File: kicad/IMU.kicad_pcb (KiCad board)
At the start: 4 copper layers, 37.6 x 37.6 mm, 89 parts, among them IC1 FT232RQ, P1 M1P, P10 CONN_01X02, P11 CONN_02X05, P12 CONN_02X06, P2 M1N, P3 M3P, P4 M3N, P5 JTAG_DB, P6 M2P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

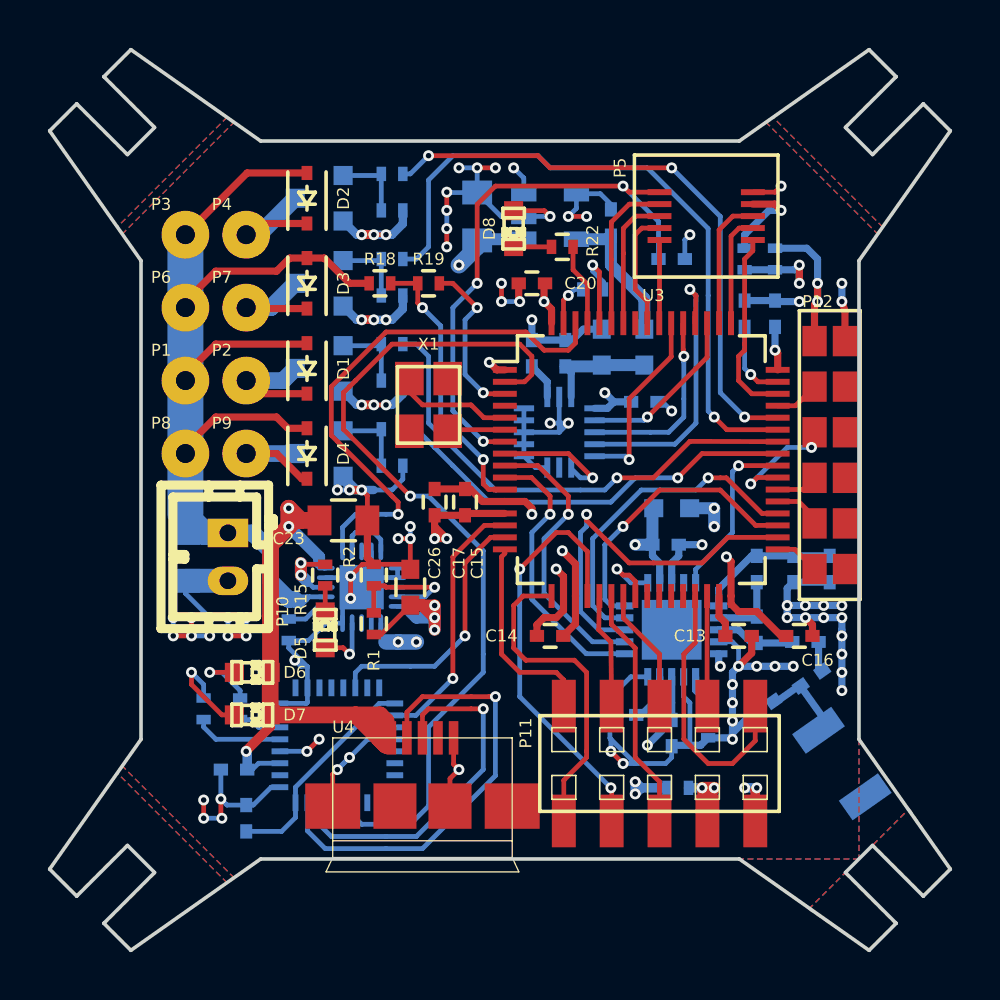
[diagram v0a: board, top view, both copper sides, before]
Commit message: Add mounting holes and XYZ-silkscreen.
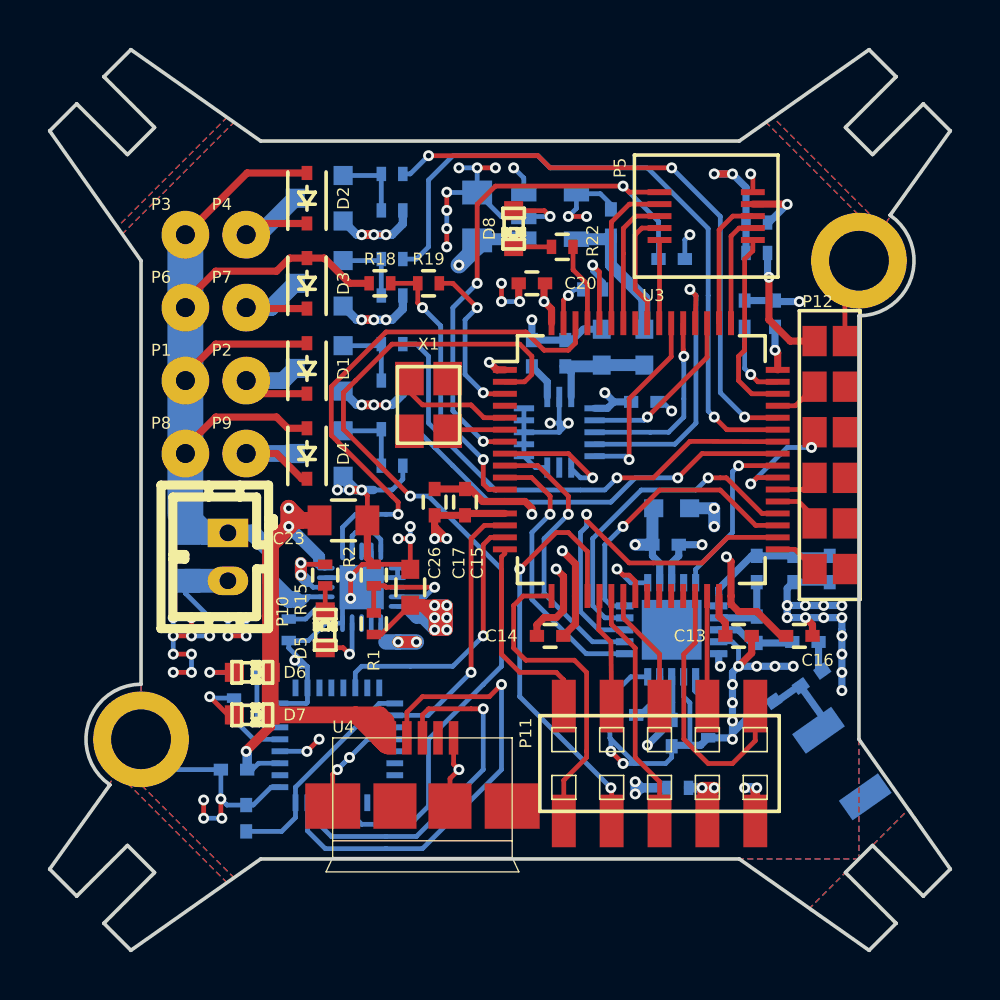
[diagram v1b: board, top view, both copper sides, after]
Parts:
- added MH1: Mounting, Mounting_Holes:MountingHole_2-5mm, F.Cu at (130.0, 75.0)
- added MH2: Mounting, Mounting_Holes:MountingHole_2-5mm, F.Cu at (100.0, 95.0)
- added REF**: coord_xyz, logos:coord_xyz, B.Cu at (117.1, 93.2)
- moved R14 1.61 mm to (125.7, 73.4), turned to 180 degrees
- moved R20 1.55 mm to (104.4, 92.2), turned to 180 degrees
- moved R21 1.27 mm to (103.9, 93.7)
- moved R17 0.80 mm to (125.7, 74.7), turned to 0 degrees
- moved G*** 0.72 mm to (128.0, 70.9)
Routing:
- net VDD: track 37.3 -> 47.9 mm, vias 17 -> 20
- net GND: track 159.6 -> 167.1 mm, vias 87 -> 89
- net Net-(D7-Pad2): track 4.11 -> 2.38 mm
- net Net-(IC1-Pad21): track 3.71 -> 2.26 mm
- net Net-(IC1-Pad22): track 1.80 -> 3.07 mm
- net Net-(P5-Pad4): track 3.80 -> 2.57 mm
- net Net-(P12-Pad1): track 6.21 -> 5.09 mm, vias 2 -> 1
- net Net-(IC1-Pad15): track 18.9 -> 20.0 mm
- net Net-(D6-Pad2): track 2.93 -> 2.10 mm
- net Net-(C25-Pad1): track 40.7 -> 41.5 mm
- net /Microcontroller/PWREN#: track 36.1 -> 36.8 mm
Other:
- outline, holes or cut-outs redrawn

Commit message: Move panda logo.
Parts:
- moved G*** 10.4 mm to (125.7, 81.0), turned to 270 degrees

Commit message: Changed R,C and D's in sch from old standard lib to new lib. Move GND-via under debug connector.
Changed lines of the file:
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@@
-(kicad_pcb (version 4) (host pcbnew "(2015-04-25 BZR 5623)-product")
+(kicad_pcb (version 4) (host pcbnew "(2015-06-20 BZR 5796)-product")
   (general
     (links 234)
@@
   (segment (start 116.975 80.06) (end 116.332 79.417) (width 0.3) (layer B.Cu) (net 1))
   (segment (start 116.975 80.694) (end 116.975 80.06) (width 0.3) (layer B.Cu) (net 1))
+  (segment (start 122.724 74.93) (end 122.724 75.396) (width 0.2) (layer B.Cu) (net 2) (status 400000))
+  (via (at 122.428 75.692) (size 0.4572) (drill 0.254) (layers F.Cu B.Cu) (net 2))
+  (segment (start 122.724 75.396) (end 122.428 75.692) (width 0.2) (layer B.Cu) (net 2))
   (segment (start 101.346 90.678) (end 101.346 91.44) (width 0.2) (layer B.Cu) (net 2))
   (via (at 101.346 91.44) (size 0.4572) (layers F.Cu B.Cu) (net 2))
@@
   (via (at 117.094 73.152) (size 0.4572) (layers F.Cu B.Cu) (net 2))
   (segment (start 117.094 73.152) (end 115.994 73.152) (width 0.2) (layer B.Cu) (net 2))
-  (segment (start 122.724 74.93) (end 122.724 74.126) (width 0.2) (layer B.Cu) (net 2))
-  (segment (start 122.724 74.126) (end 122.936 73.914) (width 0.2) (layer B.Cu) (net 2))
-  (via (at 122.936 73.914) (size 0.4572) (layers F.Cu B.Cu) (net 2))
   (segment (start 106.934 91.948) (end 106.68 91.948) (width 0.2) (layer B.Cu) (net 2))
   (segment (start 106.68 91.948) (end 106.426 91.694) (width 0.2) (layer B.Cu) (net 2))

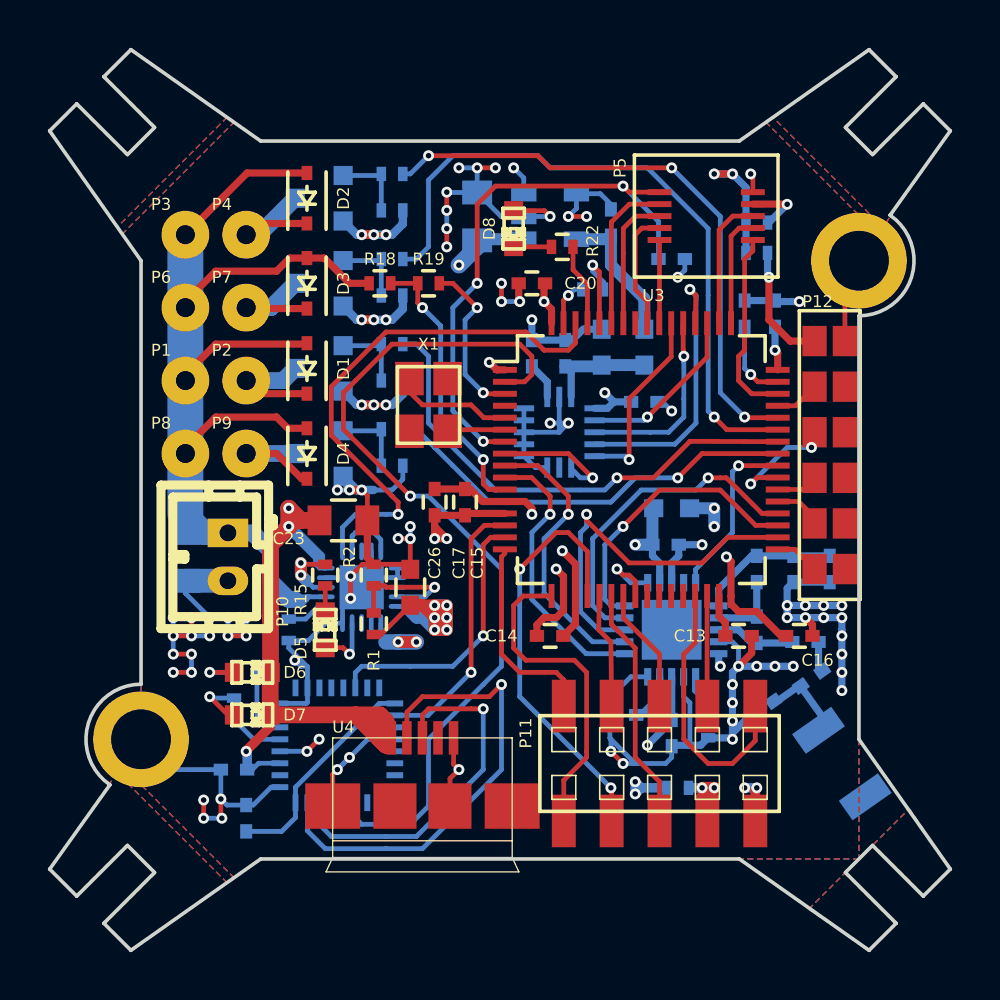
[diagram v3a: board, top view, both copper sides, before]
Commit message: Corrected ON-circuitry of LTC3553, and other minor board changes.
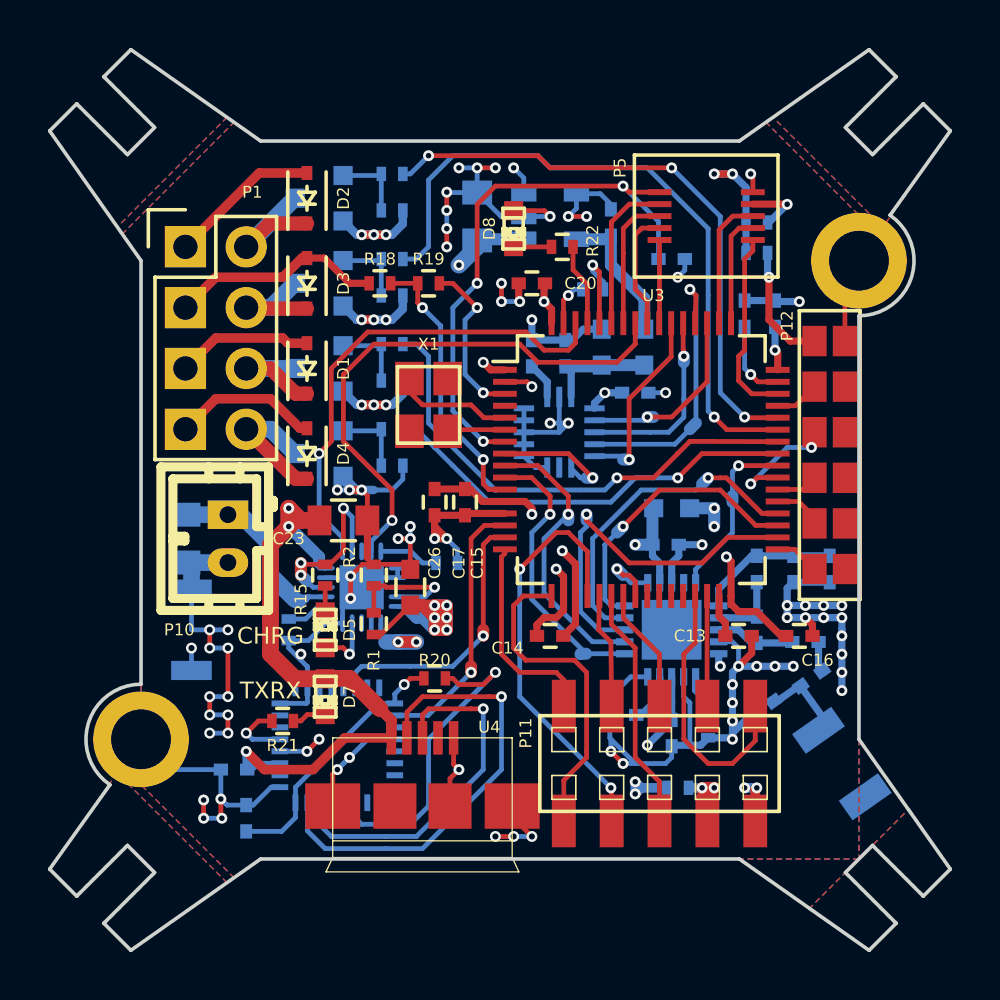
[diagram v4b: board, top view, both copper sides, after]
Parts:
- removed D6: TXLED, LEDs:LED-0603
- removed P2: M1N, Wire_Pads:SolderWirePad_single_0-8mmDrill
- removed P3: M3P, Wire_Pads:SolderWirePad_single_0-8mmDrill
- removed P4: M3N, Wire_Pads:SolderWirePad_single_0-8mmDrill
- removed P6: M2P, Wire_Pads:SolderWirePad_single_0-8mmDrill
- removed P7: M2N, Wire_Pads:SolderWirePad_single_0-8mmDrill
- removed P8: M4P, Wire_Pads:SolderWirePad_single_0-8mmDrill
- removed P9: M4N, Wire_Pads:SolderWirePad_single_0-8mmDrill
- added R23: 100k, Resistors_SMD:R_0402, B.Cu at (112.8, 87.6)
- added SW1: SW_PUSH, B3U-3000P:B3U_3000P, B.Cu at (102.1, 90.4)
- C24: value 22u -> 10u
- D7: value RXLED -> TXRXLED
- P1: value M1P -> CONN_02X04; footprint Wire_Pads:SolderWirePad_single_0-8mmDrill -> Pin_Headers:Pin_Header_Straight_2x04
- R20: value 2k2 -> 10k; moved to F.Cu
- R21: moved to F.Cu
- moved R20 7.88 mm to (112.3, 92.5), turned to 0 degrees
- moved P1 5.59 mm to (101.9, 74.4)
- moved D7 3.14 mm to (107.7, 93.2), turned to 90 degrees
- moved R21 2.09 mm to (105.9, 94.2), turned to 180 degrees
- moved C24 0.76 mm to (101.9, 86.6)
- moved P10 0.76 mm to (103.6, 86.6)
- moved C5 0.54 mm to (120.7, 80.5)
- moved G*** 0.25 mm to (125.7, 80.8)
- moved REF** 0.25 mm to (117.1, 93.5)
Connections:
- C21 pad 1: Net-(C21-Pad1) -> /Power/VccIO
- C25 pad 1: Net-(C25-Pad1) -> /Power/Vout
- D1 pad 1: Net-(D1-Pad1) -> /Microcontroller/M1N
- D2 pad 1: Net-(D2-Pad1) -> /Microcontroller/M3N
- D3 pad 1: Net-(D3-Pad1) -> /Microcontroller/M2N
- D4 pad 1: Net-(D4-Pad1) -> /Microcontroller/M4N
- D7 pad 1: +5V -> Net-(D7-Pad1)
- D7 pad 2: Net-(D7-Pad2) -> +5V
- IC1 pad 1: Net-(C21-Pad1) -> /Power/VccIO
- IC1 pad 16: Net-(C21-Pad1) -> /Power/VccIO
- Q1 pad 3: Net-(D1-Pad1) -> /Microcontroller/M1N
- Q2 pad 3: Net-(D2-Pad1) -> /Microcontroller/M3N
- Q3 pad 3: Net-(D3-Pad1) -> /Microcontroller/M2N
- Q4 pad 3: Net-(D4-Pad1) -> /Microcontroller/M4N
- R15 pad 1: Net-(C25-Pad1) -> /Power/Vout
- R20 pad 1: Net-(IC1-Pad22) -> /Power/VccIO
- R20 pad 2: Net-(D6-Pad2) -> /Microcontroller/PWREN#
- R21 pad 1: Net-(IC1-Pad21) -> Net-(D7-Pad1)
- R21 pad 2: Net-(D7-Pad2) -> Net-(IC1-Pad21)
- U3 pad 57: Net-(U3-Pad57) -> /Microcontroller/~ON
- U5 pad 11: Net-(C25-Pad1) -> /Power/Vout
- U5 pad 18: Net-(C25-Pad1) -> /Power/Vout
- U5 pad 2: Net-(U5-Pad2) -> /Power/Vout
- U5 pad 4: GND -> /Microcontroller/~ON
- U5 pad 5: Net-(U5-Pad2) -> Net-(R23-Pad1)
- U6 pad 1: Net-(C25-Pad1) -> /Power/Vout
- U6 pad 3: Net-(C25-Pad1) -> /Power/Vout
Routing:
- net /Power/Vout: track 0.00 -> 46.2 mm, vias 0 -> 7
- net Net-(C25-Pad1): track 41.5 -> 0.00 mm, vias 6 -> 0
- net /Microcontroller/~ON: track 0.00 -> 37.7 mm, vias 0 -> 2
- net /Power/VccIO: track 0.00 -> 11.0 mm, vias 0 -> 1
- net /Microcontroller/PWREN#: track 36.8 -> 27.1 mm, vias 1 -> 2
- net Net-(C21-Pad1): track 9.17 -> 0.00 mm
- net /Microcontroller/M4N: track 0.00 -> 5.87 mm
- net /Microcontroller/M3N: track 0.00 -> 5.84 mm
- net Net-(D2-Pad1): track 5.42 -> 0.00 mm
- net Net-(D3-Pad1): track 5.03 -> 0.00 mm
- net Net-(D1-Pad1): track 5.03 -> 0.00 mm
- net /Microcontroller/M2N: track 0.00 -> 5.03 mm
- net /Microcontroller/M1N: track 0.00 -> 5.03 mm
- net Net-(D4-Pad1): track 5.03 -> 0.00 mm
- net +BATT: track 53.1 -> 49.3 mm
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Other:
- board text added: "CHRG"
- board text added: "Rev B"
- board text added: "TXRX"
- board text removed: "Rev A"

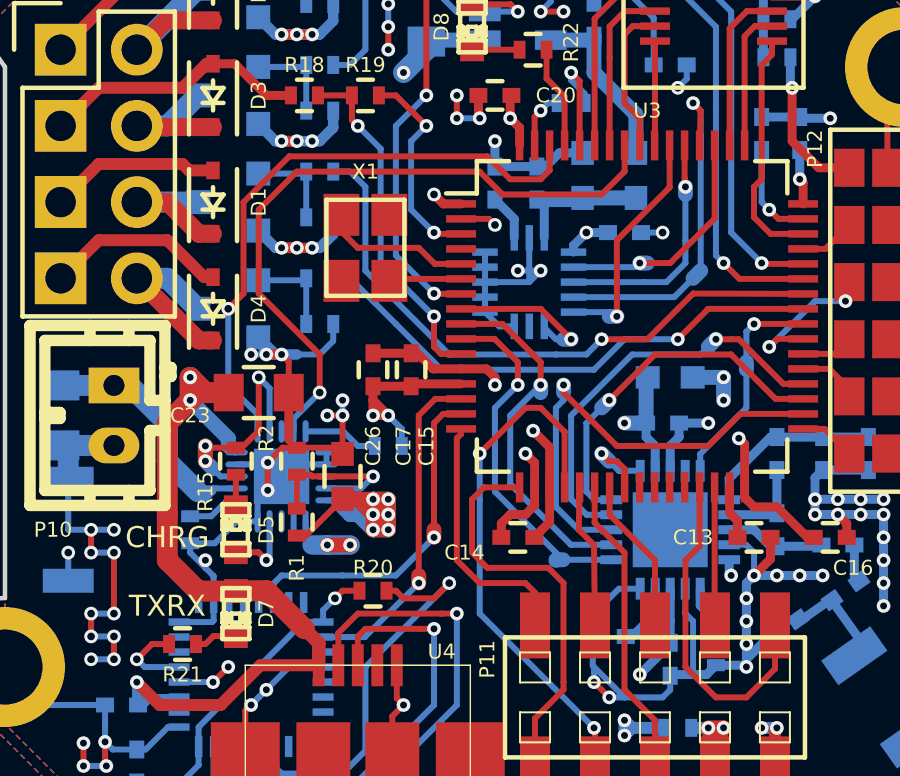
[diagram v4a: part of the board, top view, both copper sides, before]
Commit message: Connected mcu pin to LDO_ON.
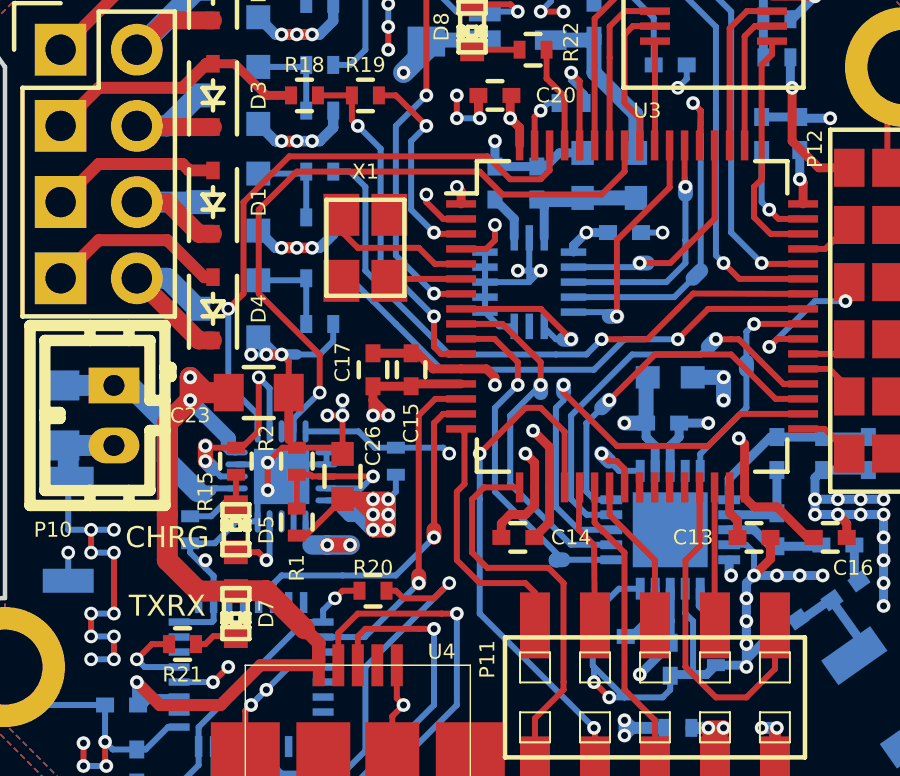
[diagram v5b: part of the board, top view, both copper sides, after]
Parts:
- moved R23 0.57 mm to (113.0, 88.1), turned to 90 degrees
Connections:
- R23 pad 1: Net-(R23-Pad1) -> VDD
- R23 pad 2: VDD -> /Microcontroller/LDO_ON
- U3 pad 2: /Microcontroller/PWREN# -> /Microcontroller/LDO_ON
- U3 pad 4: Net-(U3-Pad4) -> /Microcontroller/PWREN#
- U5 pad 5: Net-(R23-Pad1) -> /Microcontroller/LDO_ON
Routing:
- net /Microcontroller/LDO_ON: track 0.00 -> 15.9 mm, vias 0 -> 2
- net Net-(R23-Pad1): track 2.51 -> 0.00 mm
- net VDD: track 48.7 -> 48.0 mm
- net /Microcontroller/PWREN#: track 27.1 -> 27.6 mm
